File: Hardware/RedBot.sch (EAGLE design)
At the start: 62 parts, among them U1 ATMEGA328P, U2 TB6612FNG, U3 MIC5219 5V, U4 MIC5219 3.3V, U5 FT232RLSSOP, Y1 16MHz

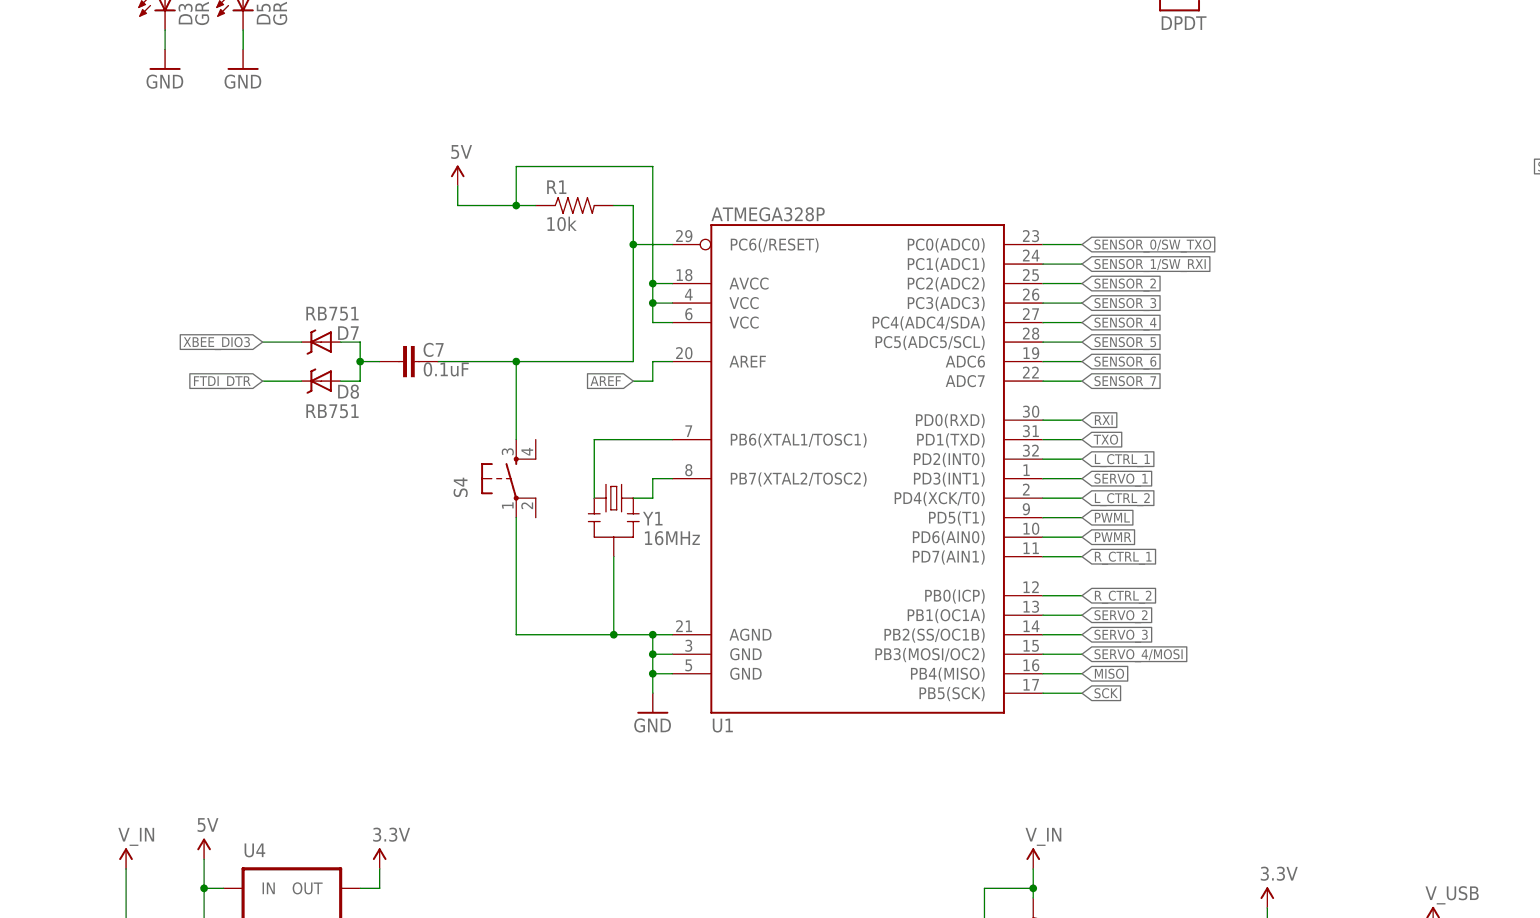
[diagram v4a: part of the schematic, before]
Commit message: Added an AND gate to the reset lines, to improve the multiplexing capabilities of the Xbee/FTDI during bootloads.
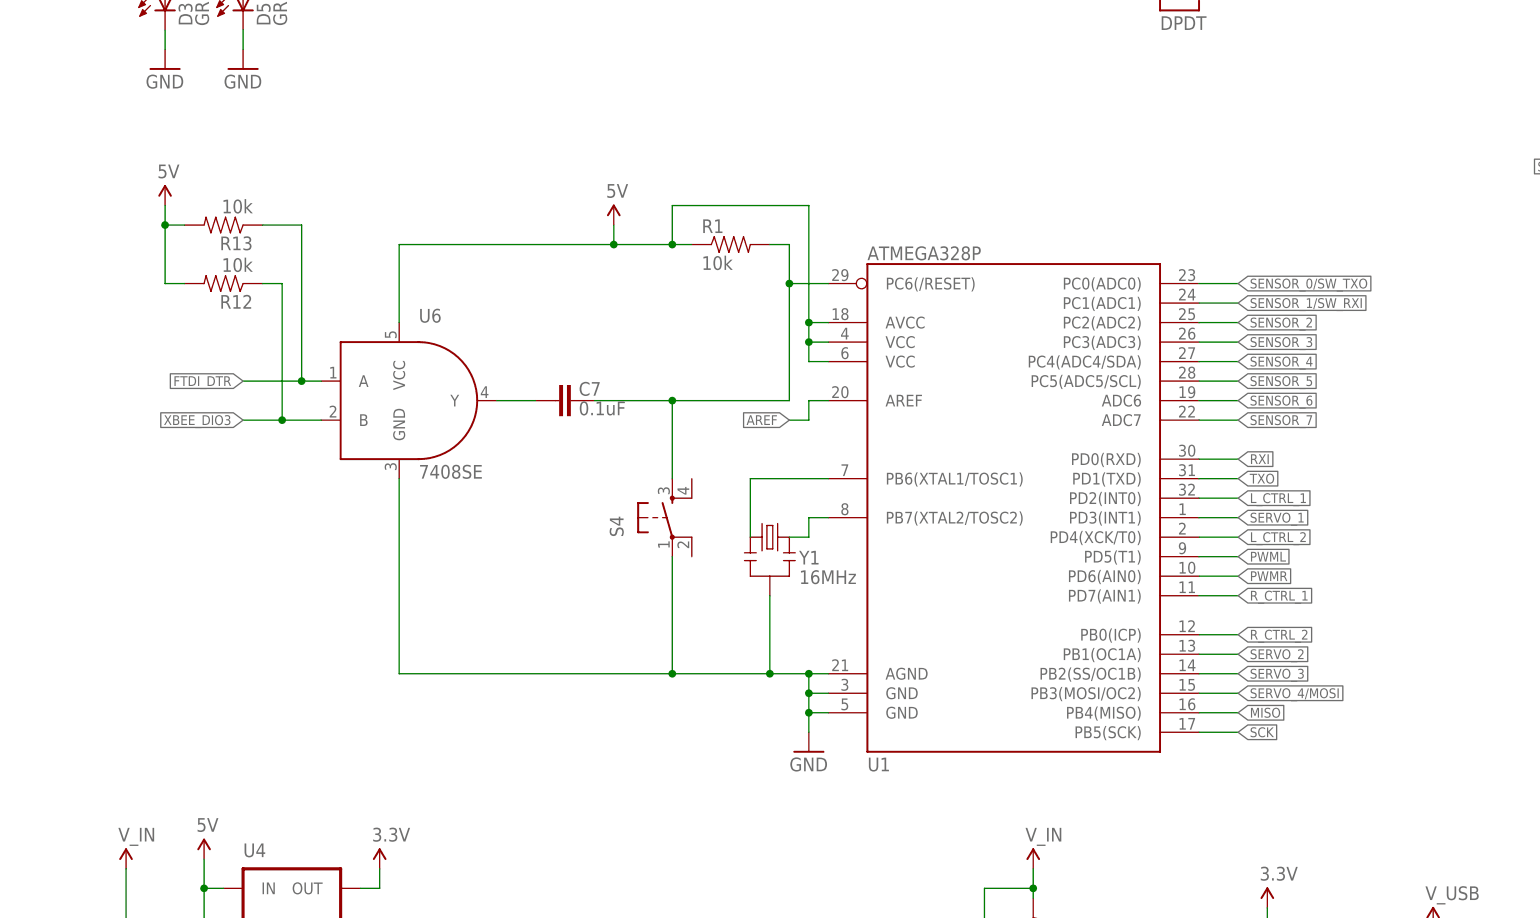
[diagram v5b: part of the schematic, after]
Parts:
- removed D7, D8: RB751, SparkFun-DiscreteSemi:RB751
- added R12, R13: 10k, SparkFun-Resistors:10KOHM1/10W1%(0603)
- added U6: 7408SE, SparkFun-DigitalIC:7408SE
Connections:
- net 5V: now also R12.2, R13.2, U6.VCC
- net FTDI_DTR: now also R13.1, U6.A; no longer D8.C
- net GND: now also U6.GND
- net N$5: now also U6.Y; no longer D7.A, D8.A
- net XBEE_DIO3: now also R12.1, U6.B; no longer D7.C
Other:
- moved on the sheet: C7, R1, S4, U1, Y1

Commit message: V03 prototypes - Added an AND gate instead of two diodes for reset control - Changed packages on the 5x2 headers along the board edges to be no silk - Moved motor header text to avoid tmask interference - Added bypass cap to FTDI chip - Grounded test pin on FTDI chip
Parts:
- JP6, JP7: value M05X2PTH -> M05X2NO_SILK; device SparkFun-Connectors:M05X2PTH -> SparkFun-Connectors:M05X2NO_SILK
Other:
- note added: "03"
- note removed: "10"
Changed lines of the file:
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@@
 <grid distance="0.1" unitdist="inch" unit="inch" style="lines" multiple="1" display="no" altdistance="0.01" altunitdist="inch" altunit="inch"/>
 <layers>
-<layer number="1" name="Top" color="4" fill="1" visible="no" active="no"/>
-<layer number="2" name="Route2" color="1" fill="3" visible="no" active="no"/>
-<layer number="3" name="Route3" color="4" fill="3" visible="no" active="no"/>
-<layer number="4" name="Route4" color="1" fill="4" visible="no" active="no"/>
-<layer number="5" name="Route5" color="4" fill="4" visible="no" active="no"/>
-<layer number="6" name="Route6" color="1" fill="8" visible="no" active="no"/>
-<layer number="7" name="Route7" color="4" fill="8" visible="no" active="no"/>
-<layer number="8" name="Route8" color="1" fill="2" visible="no" active="no"/>
-<layer number="9" name="Route9" color="4" fill="2" visible="no" active="no"/>
-<layer number="10" name="Route10" color="1" fill="7" visible="no" active="no"/>
-<layer number="11" name="Route11" color="4" fill="7" visible="no" active="no"/>
-<layer number="12" name="Route12" color="1" fill="5" visible="no" active="no"/>
-<layer number="13" name="Route13" color="4" fill="5" visible="no" active="no"/>
-<layer number="14" name="Route14" color="1" fill="6" visible="no" active="no"/>
-<layer number="15" name="Route15" color="4" fill="6" visible="no" active="no"/>
-<layer number="16" name="Bottom" color="1" fill="1" visible="no" active="no"/>
-<layer number="17" name="Pads" color="2" fill="1" visible="no" active="no"/>
-<layer number="18" name="Vias" color="2" fill="1" visible="no" active="no"/>
-<layer number="19" name="Unrouted" color="6" fill="1" visible="no" active="no"/>
-<layer number="20" name="Dimension" color="15" fill="1" visible="no" active="no"/>
-<layer number="21" name="tPlace" color="16" fill="1" visible="no" active="no"/>
-<layer number="22" name="bPlace" color="14" fill="1" visible="no" active="no"/>
-<layer number="23" name="tOrigins" color="15" fill="1" visible="no" active="no"/>
-<layer number="24" name="bOrigins" color="15" fill="1" visible="no" active="no"/>
-<layer number="25" name="tNames" color="7" fill="1" visible="no" active="no"/>
-<layer number="26" name="bNames" color="7" fill="1" visible="no" active="no"/>
-<layer number="27" name="tValues" color="7" fill="1" visible="no" active="no"/>
-<layer number="28" name="bValues" color="7" fill="1" visible="no" active="no"/>
+<layer number="1" name="Top" color="4" fill="1" visible="yes" active="no"/>
+<layer number="2" name="Route2" color="1" fill="3" visible="yes" active="no"/>
+<layer number="3" name="Route3" color="4" fill="3" visible="yes" active="no"/>
+<layer number="4" name="Route4" color="1" fill="4" visible="yes" active="no"/>
+<layer number="5" name="Route5" color="4" fill="4" visible="yes" active="no"/>
+<layer number="6" name="Route6" color="1" fill="8" visible="yes" active="no"/>
+<layer number="7" name="Route7" color="4" fill="8" visible="yes" active="no"/>
+<layer number="8" name="Route8" color="1" fill="2" visible="yes" active="no"/>
+<layer number="9" name="Route9" color="4" fill="2" visible="yes" active="no"/>
+<layer number="10" name="Route10" color="1" fill="7" visible="yes" active="no"/>
+<layer number="11" name="Route11" color="4" fill="7" visible="yes" active="no"/>
+<layer number="12" name="Route12" color="1" fill="5" visible="yes" active="no"/>
+<layer number="13" name="Route13" color="4" fill="5" visible="yes" active="no"/>
+<layer number="14" name="Route14" color="1" fill="6" visible="yes" active="no"/>
+<layer number="15" name="Route15" color="4" fill="6" visible="yes" active="no"/>
+<layer number="16" name="Bottom" color="1" fill="1" visible="yes" active="no"/>
+<layer number="17" name="Pads" color="2" fill="1" visible="yes" active="no"/>
+<layer number="18" name="Vias" color="2" fill="1" visible="yes" active="no"/>
+<layer number="19" name="Unrouted" color="6" fill="1" visible="yes" active="no"/>
+<layer number="20" name="Dimension" color="15" fill="1" visible="yes" active="no"/>
+<layer number="21" name="tPlace" color="16" fill="1" visible="yes" active="no"/>
+<layer number="22" name="bPlace" color="14" fill="1" visible="yes" active="no"/>
+<layer number="23" name="tOrigins" color="15" fill="1" visible="yes" active="no"/>
+<layer number="24" name="bOrigins" color="15" fill="1" visible="yes" active="no"/>
+<layer number="25" name="tNames" color="7" fill="1" visible="yes" active="no"/>
+<layer number="26" name="bNames" color="7" fill="1" visible="yes" active="no"/>
+<layer number="27" name="tValues" color="7" fill="1" visible="yes" active="no"/>
+<layer number="28" name="bValues" color="7" fill="1" visible="yes" active="no"/>
 <layer number="29" name="tStop" color="7" fill="3" visible="no" active="no"/>
 <layer number="30" name="bStop" color="7" fill="6" visible="no" active="no"/>
@@
 <layer number="35" name="tGlue" color="7" fill="4" visible="no" active="no"/>
 <layer number="36" name="bGlue" color="7" fill="5" visible="no" active="no"/>
-<layer number="37" name="tTest" color="7" fill="1" visible="no" active="no"/>
-<layer number="38" name="bTest" color="7" fill="1" visible="no" active="no"/>
+<layer number="37" name="tTest" color="7" fill="1" visible="yes" active="no"/>
+<layer number="38" name="bTest" color="7" fill="1" visible="yes" active="no"/>
 <layer number="39" name="tKeepout" color="4" fill="11" visible="no" active="no"/>
 <layer number="40" name="bKeepout" color="1" fill="11" visible="no" active="no"/>
@@
 <layer number="44" name="Drills" color="7" fill="1" visible="no" active="no"/>
 <layer number="45" name="Holes" color="7" fill="1" visible="no" active="no"/>
-<layer number="46" name="Milling" color="3" fill="1" visible="no" active="no"/>
-<layer number="47" name="Measures" color="7" fill="1" visible="no" active="no"/>
-<layer number="48" name="Document" color="7" fill="1" visible="no" active="no"/>
-<layer number="49" name="Reference" color="7" fill="1" visible="no" active="no"/>
-<layer number="50" name="dxf" color="7" fill="1" visible="no" active="no"/>
-<layer number="51" name="tDocu" color="6" fill="1" visible="no" active="no"/>
-<layer number="52" name="bDocu" color="7" fill="1" visible="no" active="no"/>
-<layer number="53" name="tGND_GNDA" color="7" fill="9" visible="no" active="no"/>
-<layer number="54" name="bGND_GNDA" color="1" fill="9" visible="no" active="no"/>
-<layer number="56" name="wert" color="7" fill="1" visible="no" active="no"/>
+<layer number="46" name="Milling" color="3" fill="1" visible="yes" active="no"/>
+<layer number="47" name="Measures" color="7" fill="1" visible="yes" active="no"/>
+<layer number="48" name="Document" color="7" fill="1" visible="yes" active="no"/>
+<layer number="49" name="Reference" color="7" fill="1" visible="yes" active="no"/>
+<layer number="50" name="dxf" color="7" fill="1" visible="yes" active="no"/>
+<layer number="51" name="tDocu" color="6" fill="1" visible="yes" active="no"/>
+<layer number="52" name="bDocu" color="7" fill="1" visible="yes" active="no"/>
+<layer number="53" name="tGND_GNDA" color="7" fill="9" visible="yes" active="no"/>
+<layer number="54" name="bGND_GNDA" color="1" fill="9" visible="yes" active="no"/>
+<layer number="56" name="wert" color="7" fill="1" visible="yes" active="no"/>
 <layer number="91" name="Nets" color="2" fill="1" visible="yes" active="yes"/>
 <layer number="92" name="Busses" color="1" fill="1" visible="yes" active="yes"/>
@@
 <attribute name="VALUE" value="1k"/>
 </part>
-<part name="JP6" library="SparkFun-Connectors" deviceset="M05X2" device="PTH" value="M05X2PTH"/>
-<part name="JP7" library="SparkFun-Connectors" deviceset="M05X2" device="PTH" value="M05X2PTH"/>
+<part name="JP6" library="SparkFun-Connectors" deviceset="M05X2" device="NO_SILK" value="M05X2NO_SILK"/>
+<part name="JP7" library="SparkFun-Connectors" deviceset="M05X2" device="NO_SILK" value="M05X2NO_SILK"/>
 <part name="U$15" library="SparkFun-Aesthetics" deviceset="5V" device=""/>
 <part name="U$16" library="SparkFun-Aesthetics" deviceset="5V" device=""/>
@@
 <wire x1="0" y1="254" x2="0" y2="0" width="0.1524" layer="94"/>
 <text x="330.2" y="7.62" size="5.08" layer="94">M.Hord</text>
-<text x="395.986" y="6.35" size="3.81" layer="94">10</text>
+<text x="395.986" y="6.35" size="3.81" layer="94">03</text>
 </plain>
 <instances>

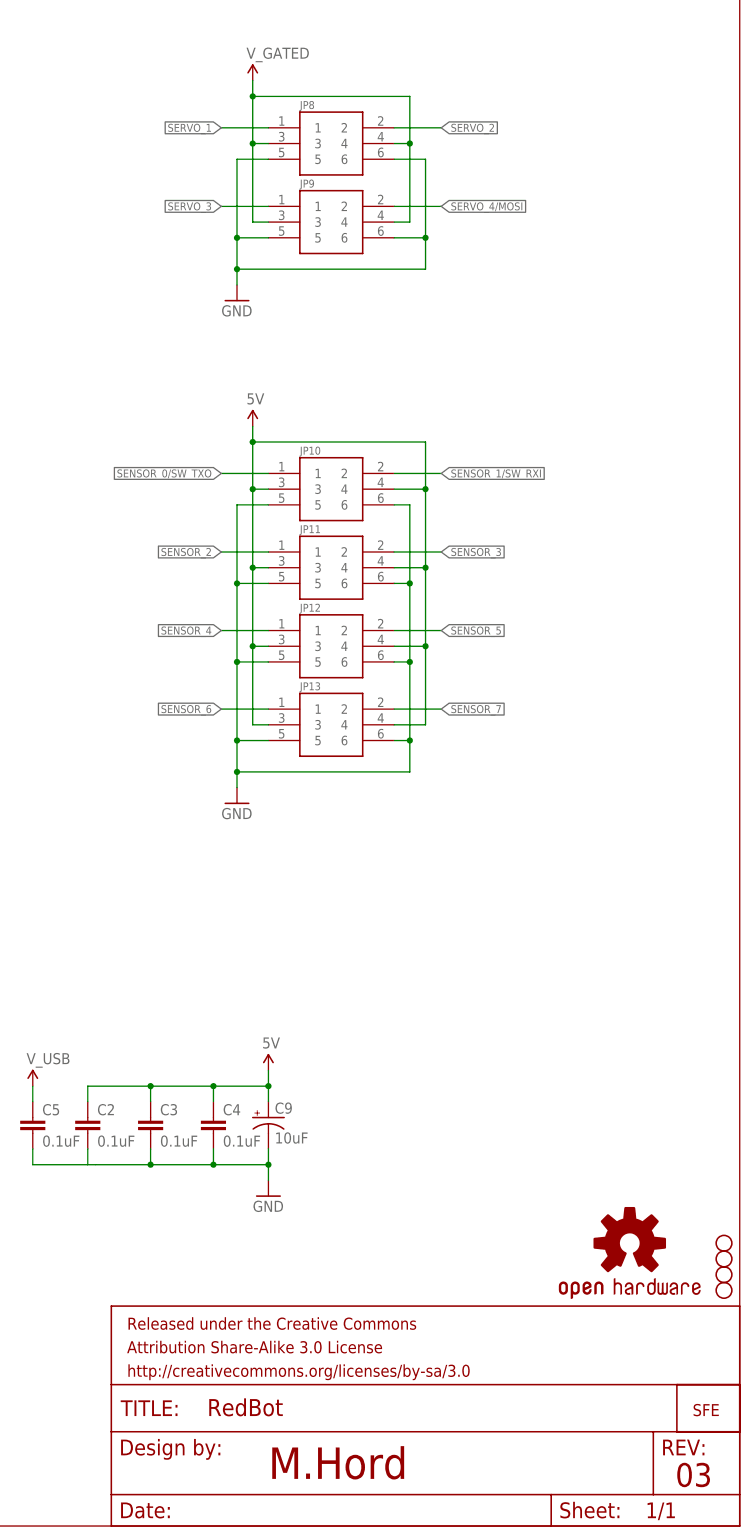
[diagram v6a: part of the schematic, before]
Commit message: Change board/schematic to v10  - Tweaks to board labels  - Change as many 0.015" vias to 0.020" as possible.  - Address a few minor clearance issues.
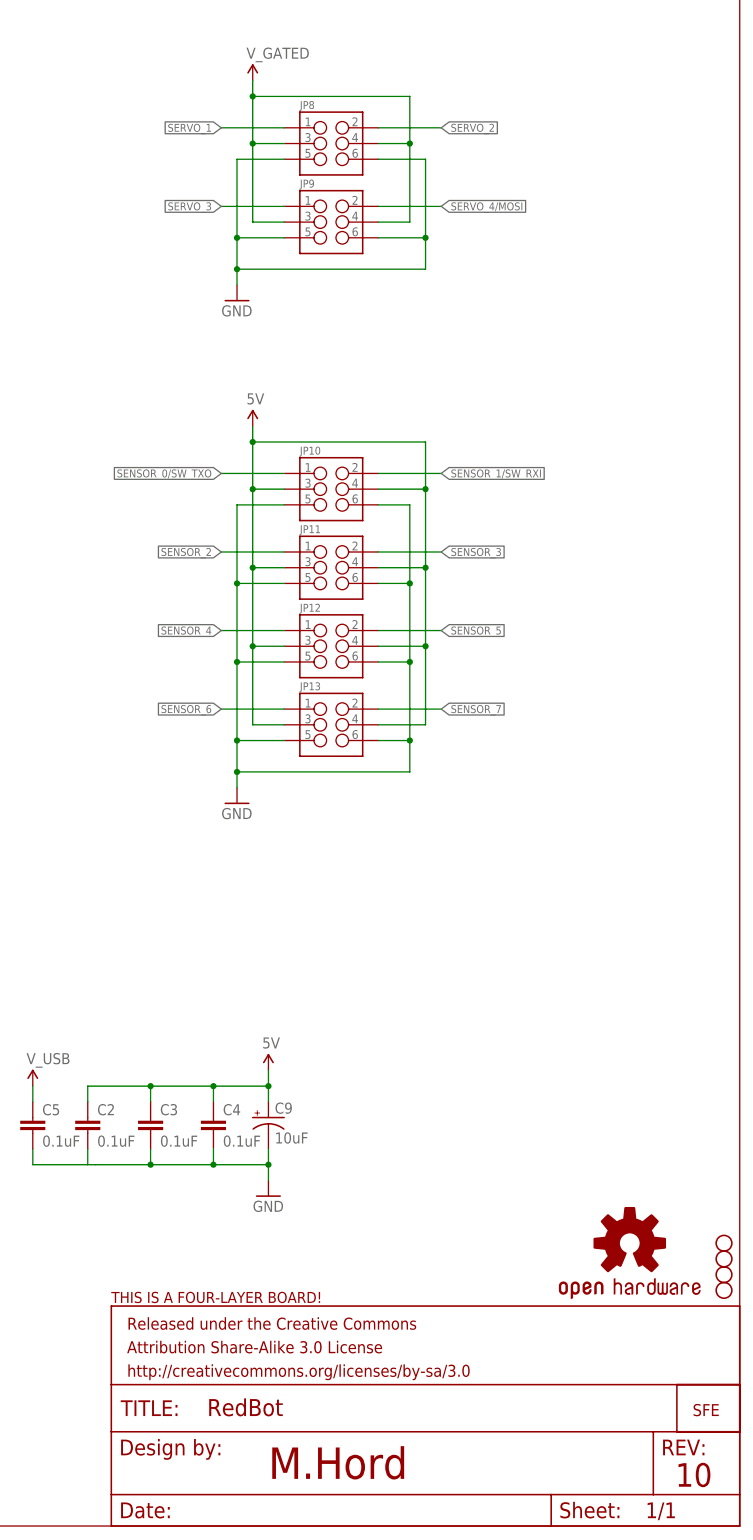
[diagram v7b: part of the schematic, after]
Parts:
- added U$21: FOUR_LAYER_WARNING, SparkFun-Aesthetics:FOUR_LAYER_WARNING
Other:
- note added: "10"
- note removed: "03"

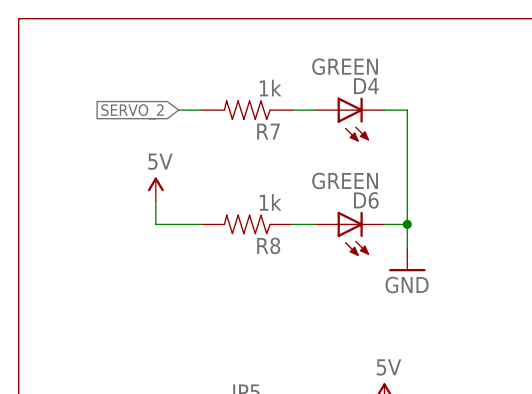
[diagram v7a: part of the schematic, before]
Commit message: Moved User LED to pin 13
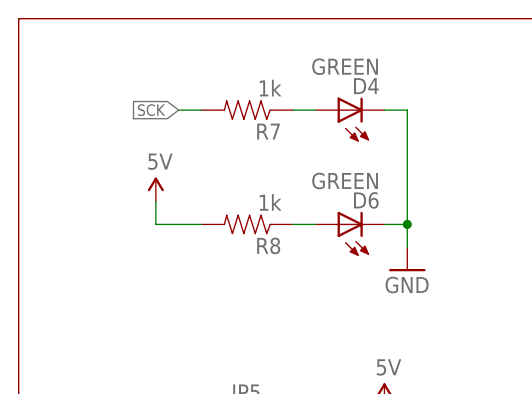
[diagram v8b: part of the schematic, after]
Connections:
- net SCK: now also R7.2
- net SERVO_2: no longer R7.2
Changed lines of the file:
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@@
 <label x="358.14" y="226.06" size="1.27" layer="95" xref="yes"/>
-</segment>
-<segment>
-<pinref part="R7" gate="G$1" pin="2"/>
-<wire x1="20.32" y1="243.84" x2="17.78" y2="243.84" width="0.1524" layer="91"/>
-<label x="17.78" y="243.84" size="1.27" layer="95" rot="R180" xref="yes"/>
 </segment>
 </net>
@@
 <label x="15.24" y="205.74" size="1.27" layer="95" rot="R180" xref="yes"/>
 </segment>
+<segment>
+<pinref part="R7" gate="G$1" pin="2"/>
+<wire x1="20.32" y1="243.84" x2="17.78" y2="243.84" width="0.1524" layer="91"/>
+<label x="17.78" y="243.84" size="1.27" layer="95" rot="R180" xref="yes"/>
+</segment>
 </net>
